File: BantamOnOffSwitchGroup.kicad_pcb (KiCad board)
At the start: 2 copper layers, 14.6 x 34 mm, 4 parts, among them J1 Conn_01x02_Male, J2 Conn_01x04_Male, SW1 SW_Push_DPDT

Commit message: added copper pour, need to doublecheck measurements
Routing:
- added copper zone on B.Cu, net Net-(D1-Pad1)
- added copper zone on F.Cu, net Net-(D1-Pad1)
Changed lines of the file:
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@@
 		(net 5)
 	)
+	(zone
+		(net 1)
+		(net_name "Net-(D1-Pad1)")
+		(layers "F&B.Cu")
+		(hatch edge 0.5)
+		(connect_pads thru_hole_only
+			(clearance 0.508)
+		)
+		(min_thickness 0.25)
+		(filled_areas_thickness no)
+		(fill yes
+			(thermal_gap 0.5)
+			(thermal_bridge_width 0.5)
+			(island_removal_mode 1)
+			(island_area_min 10)
+		)
+		(polygon
+			(pts
+				(xy 139.95 83.75) (xy 154.5 83.75) (xy 154.55 117.75) (xy 140 117.7)
+			)
+		)
+	)
 )

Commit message: gbr and drill files created
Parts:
- moved D1 10.2 mm to (136.2, 103.1)
- moved J1 10.2 mm to (138.8, 110.3)
- moved SW1 10.2 mm to (137.5, 86.2)
- moved J2 10.2 mm to (133.6, 95.1)
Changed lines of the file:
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@@
 		(legacy_teardrops no)
 	)
-	(paper "A4")
+	(paper "A")
+	(title_block
+		(title "Bantamp Power Switch Group")
+		(date "2024-03-06")
+		(company "RoboWidgets")
+	)
 	(layers
 		(0 "F.Cu" signal)
@@
 			(outputformat 1)
 			(mirror no)
-			(drillshape 1)
+			(drillshape 0)
 			(scaleselection 1)
-			(outputdirectory "")
+			(outputdirectory "ouput/")
 		)
 	)
@@
 	(footprint "Connector_PinHeader_2.54mm:PinHeader_1x04_P2.54mm_Vertical"
 		(layer "F.Cu")
-		(at 143.2 98.4 90)
+		(at 133.551824 95.090218 90)
 		(descr "Through hole straight pin header, 1x04, 2.54mm pitch, single row")
 		(tags "Through hole pin header THT 1x04 2.54mm single row")
@@
 	(footprint "LED_THT:LED_D3.0mm"
 		(layer "F.Cu")
-		(at 145.86 106.3845)
+		(at 136.211824 103.074718)
 		(descr "LED, diameter 3.0mm, 2 pins")
 		(tags "LED diameter 3.0mm 2 pins")
@@
 	(footprint "Connector_PinHeader_2.54mm:PinHeader_1x02_P2.54mm_Vertical"
 		(layer "F.Cu")
-		(at 148.4 113.6 -90)
+		(at 138.751824 110.290218 -90)
 		(descr "Through hole straight pin header, 1x02, 2.54mm pitch, single row")
 		(tags "Through hole pin header THT 1x02 2.54mm single row")
@@
 	(footprint "Kidwidgets:Toggle_DPDT"
 		(layer "F.Cu")
-		(at 147.193 89.535)
+		(at 137.544824 86.225218)
 		(property "Reference" "SW1"
 			(at 0.127 -5.08 0)
@@
 	)
 	(gr_rect
-		(start 139.9 83.8)
-		(end 154.5 117.8)
+		(start 130.251824 80.490218)
+		(end 144.851824 114.490218)
 		(stroke
 			(width 0.1)
@@
 	)
 	(segment
-		(start 145.86 106.3845)
-		(end 145.86 113.6)
+		(start 136.211824 103.074718)
+		(end 136.211824 110.290218)
 		(width 1)
 		(layer "B.Cu")
@@
 	)
 	(segment
-		(start 148.4 106.3845)
-		(end 148.4 113.6)
+		(start 138.751824 103.074718)
+		(end 138.751824 110.290218)
 		(width 1)
 		(layer "B.Cu")
@@
 	)
 	(segment
-		(start 143.2 98.4)
-		(end 145.74 98.4)
+		(start 133.551824 95.090218)
+		(end 136.091824 95.090218)
 		(width 1)
 		(layer "B.Cu")
@@
 	)
 	(segment
-		(start 144.78 89.535)
-		(end 142.315 89.535)
+		(start 135.131824 86.225218)
+		(end 132.666824 86.225218)
 		(width 1)
 		(layer "B.Cu")
@@
 	)
 	(segment
-		(start 141.35 97.85)
-		(end 141.9 98.4)
+		(start 131.701824 94.540218)
+		(end 132.251824 95.090218)
 		(width 1)
 		(layer "B.Cu")
@@
 	)
 	(segment
-		(start 142.315 89.535)
-		(end 141.35 90.5)
+		(start 132.666824 86.225218)
+		(end 131.701824 87.190218)
 		(width 1)
 		(layer "B.Cu")
@@
 	)
 	(segment
-		(start 149.606 89.535)
-		(end 144.78 89.535)
+		(start 139.957824 86.225218)
+		(end 135.131824 86.225218)
 		(width 1)
 		(layer "B.Cu")
@@
 	)
 	(segment
-		(start 141.35 90.5)
-		(end 141.35 97.85)
+		(start 131.701824 87.190218)
+		(end 131.701824 94.540218)
 		(width 1)
 		(layer "B.Cu")
@@
 	)
 	(segment
-		(start 141.9 98.4)
-		(end 143.2 98.4)
+		(start 132.251824 95.090218)
+		(end 133.551824 95.090218)
 		(width 1)
 		(layer "B.Cu")
@@
 	)
 	(segment
-		(start 151.6 98.4)
-		(end 150.82 98.4)
+		(start 141.951824 95.090218)
+		(end 141.171824 95.090218)
 		(width 0.25)
 		(layer "F.Cu")
@@
 	)
 	(segment
-		(start 151.5855 87.1855)
-		(end 153.15 88.75)
+		(start 141.937324 83.875718)
+		(end 143.501824 85.440218)
 		(width 1)
 		(layer "B.Cu")
@@
 	)
 	(segment
-		(start 153.15 88.75)
-		(end 153.15 97.3)
+		(start 143.501824 85.440218)
+		(end 143.501824 93.990218)
 		(width 1)
 		(layer "B.Cu")
@@
 	)
 	(segment
-		(start 153.15 97.3)
-		(end 152.05 98.4)
+		(start 143.501824 93.990218)
+		(end 142.401824 95.090218)
 		(width 1)
 		(layer "B.Cu")
@@
 	)
 	(segment
-		(start 152.05 98.4)
-		(end 150.82 98.4)
+		(start 142.401824 95.090218)
+		(end 141.171824 95.090218)
 		(width 1)
 		(layer "B.Cu")
@@
 	)
 	(segment
-		(start 144.78 87.1855)
-		(end 149.606 87.1855)
+		(start 135.131824 83.875718)
+		(end 139.957824 83.875718)
 		(width 1)
 		(layer "B.Cu")
@@
 	)
 	(segment
-		(start 148.28 98.4)
-		(end 150.82 98.4)
+		(start 138.631824 95.090218)
+		(end 141.171824 95.090218)
 		(width 1)
 		(layer "B.Cu")
@@
 	)
 	(segment
-		(start 149.606 87.1855)
-		(end 151.5855 87.1855)
+		(start 139.957824 83.875718)
+		(end 141.937324 83.875718)
 		(width 1)
 		(layer "B.Cu")
@@
 	)
 	(segment
-		(start 144.78 91.8845)
-		(end 149.606 91.8845)
+		(start 135.131824 88.574718)
+		(end 139.957824 88.574718)
 		(width 1)
 		(layer "B.Cu")
@@
 		(polygon
 			(pts
-				(xy 139.95 83.75) (xy 154.5 83.75) (xy 154.55 117.75) (xy 140 117.7)
-			)
-		)
+				(xy 130.301824 80.440218) (xy 144.851824 80.440218) (xy 144.901824 114.440218) (xy 130.351824 114.390218)
+			)
+		)

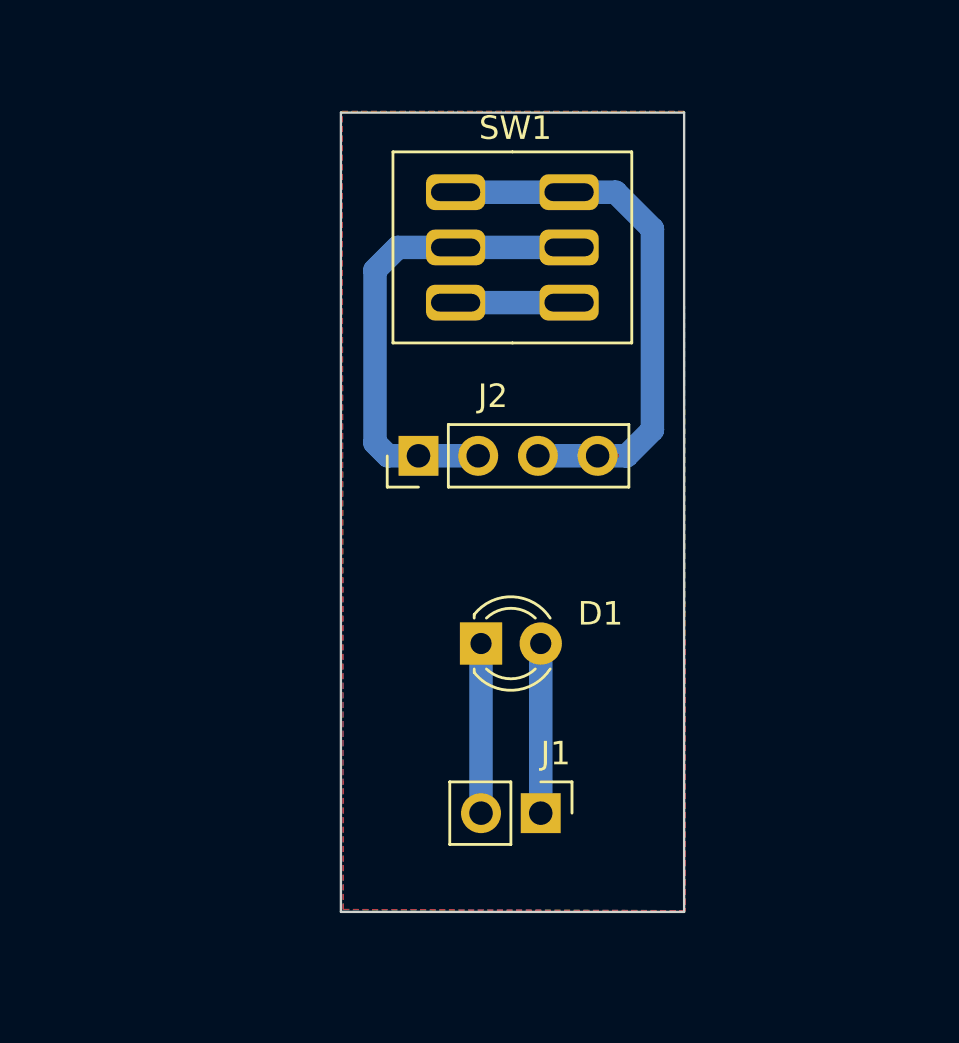
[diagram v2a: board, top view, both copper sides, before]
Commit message: fixed spacing on switch legs
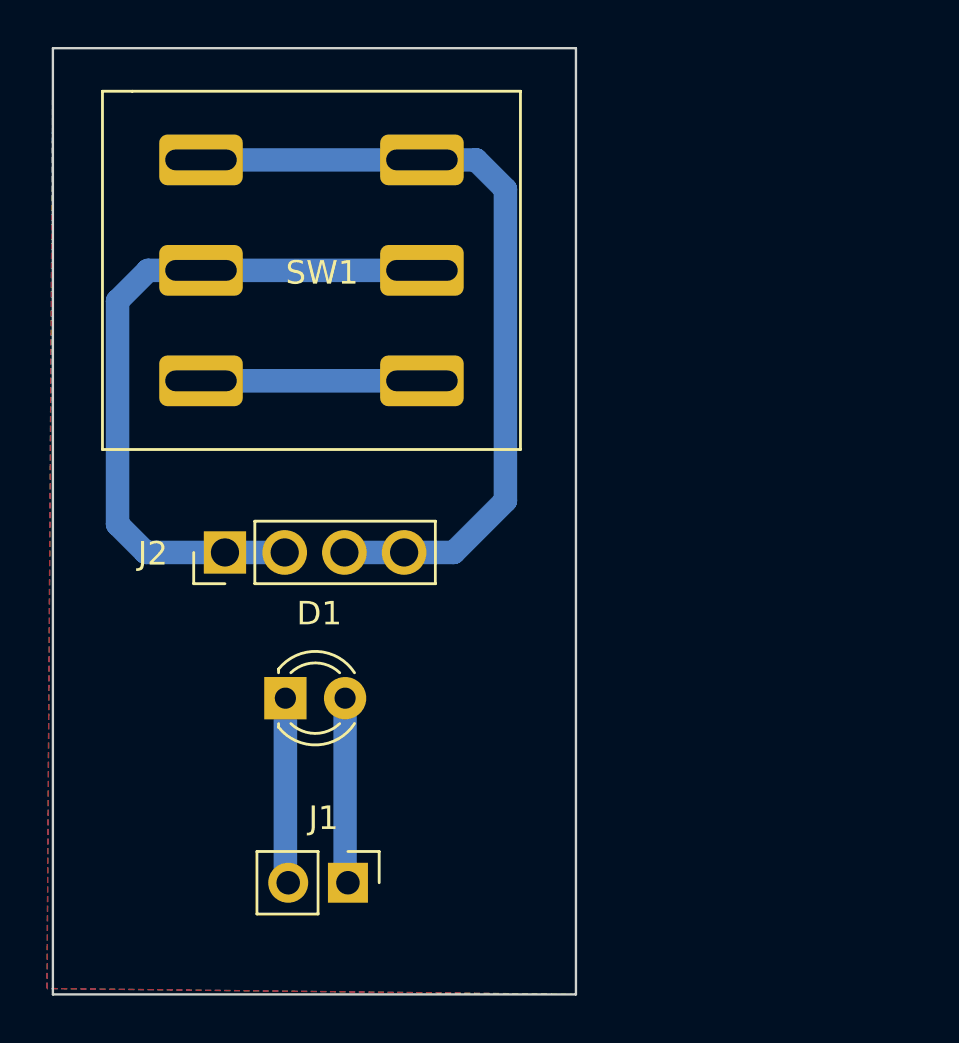
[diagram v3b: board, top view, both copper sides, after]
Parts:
- moved J2 9.20 mm to (125.3, 99.2)
- moved J1 8.72 mm to (130.6, 113.2)
- moved D1 8.64 mm to (127.9, 105.4)
- moved SW1 8.60 mm to (129.0, 87.2)
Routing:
- net Net-(J2-Pin_3): track 23.7 -> 34.5 mm
- net Net-(J2-Pin_1): track 20.6 -> 30.6 mm
- net Net-(SW1-C-Pad3): track 4.83 -> 9.40 mm
- net Net-(D1-A): track 7.22 -> 7.90 mm
- net Net-(D1-K): track 7.22 -> 7.90 mm
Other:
- board size 14.6 x 34 mm -> 22.2 x 40.2 mm

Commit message: fixed spacing on switch legs, twice
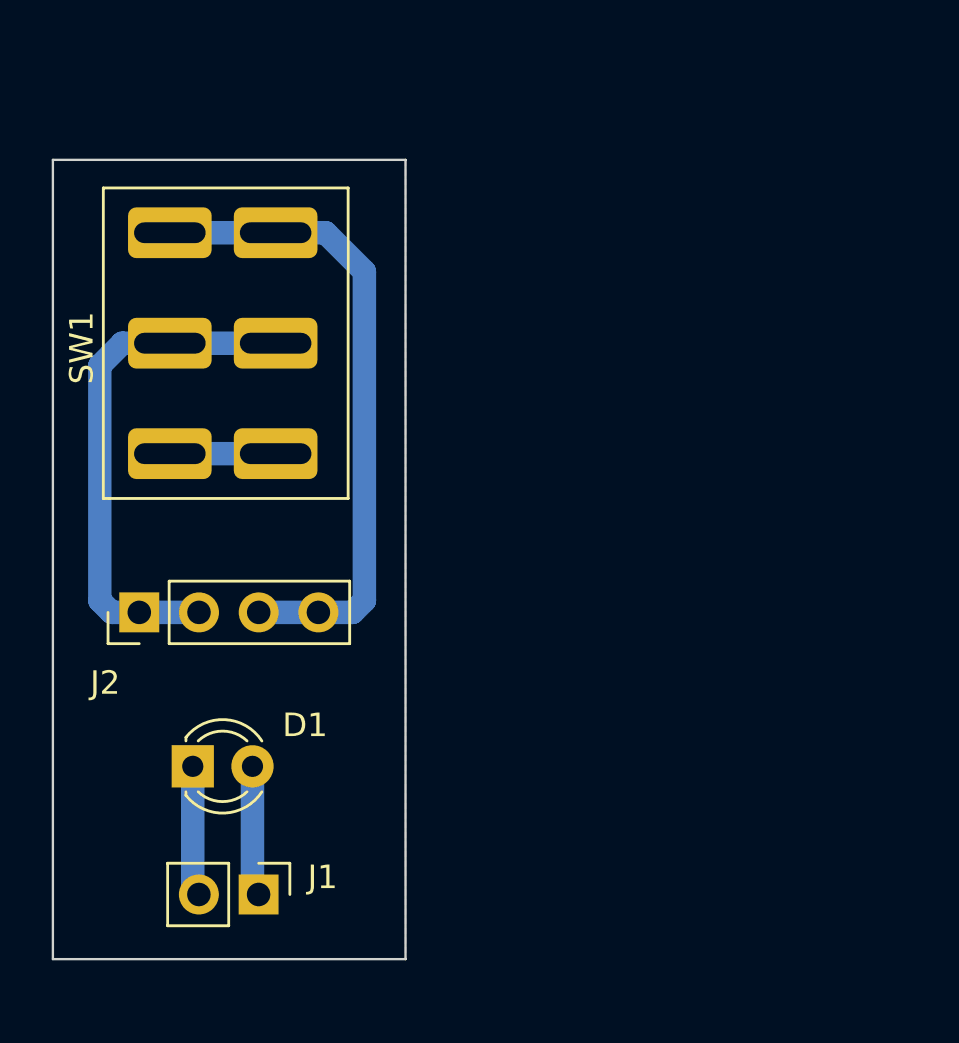
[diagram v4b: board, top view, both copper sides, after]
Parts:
- moved D1 4.89 mm to (124.0, 108.3)
- moved SW1 4.88 mm to (125.2, 90.3)
- moved J2 4.45 mm to (121.7, 101.8)
- moved J1 3.83 mm to (126.8, 113.8)
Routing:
- net Net-(J2-Pin_1): track 30.6 -> 22.3 mm
- net Net-(J2-Pin_3): track 34.5 -> 27.7 mm
- net Net-(SW1-C-Pad3): track 9.40 -> 4.50 mm
- net Net-(D1-K): track 7.90 -> 5.56 mm
- net Net-(D1-A): track 7.90 -> 5.56 mm
- added copper zone on B.Cu, net Net-(D1-A)
- added copper zone on F.Cu, net Net-(D1-A)
- removed copper zone on B.Cu, net Net-(D1-K)
- removed copper zone on F.Cu, net Net-(D1-K)
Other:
- board size 22.2 x 40.2 mm -> 15 x 34 mm
